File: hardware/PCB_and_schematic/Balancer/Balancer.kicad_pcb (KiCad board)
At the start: 2 copper layers, 99.5 x 99.5 mm, 164 parts, among them J1 BATT_OUT, J10 RS485, J11 HEATSING_TEMP1, J12 External Current Shunt, J13 BATT_IN, J2 Conn_01x04, J3 Conn_01x03, J4 HEATSING_TEMP1, J5 FAN1, J6 FAN2, J7 BATT_12V, J8 ICP, Q1 BC817, Q10 NPN, Q11 NPN, Q12 BC817, Q13 BD238, Q14 NPN, Q15 NPN, Q16 BD238, Q17 BC817, Q18 BC817, Q19 BC817, Q2 BC337, Q20 BC817, Q3 BC327, Q4 PMOS, Q5 PMOS, Q6 BC337, Q7 BC327, Q8 BC817, Q9 BC817, U1 LM324, U2 LM324, U3 LM358, U4 PIC16F886-IP, U5 TL431LP, U6 ST485, U7 INA226

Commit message: PCB UPDATE
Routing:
- net Net-(Q14-E): track 52.1 -> 52.9 mm
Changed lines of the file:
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@@
 			(xy 223.9518 54.9656) (xy 226.1616 54.9656) (xy 228.5238 57.3278) (xy 228.5238 66.1416) (xy 233.6292 71.247)
 			(xy 235.6866 71.247) (xy 235.7374 71.1962) (xy 235.7374 67.691) (xy 235.1278 67.691) (xy 232.1052 64.6684)
-			(xy 232.1052 59.8678) (xy 232.1306 59.8424) (xy 235.839 59.8424) (xy 235.839 57.3024) (xy 235.7882 57.2516)
+			(xy 232.1052 59.8678) (xy 232.1306 59.8424) (xy 232.119 59.8424) (xy 232.119 57.33) (xy 232.06 57.2516)
 			(xy 232.156 57.2516) (xy 232.1306 57.277) (xy 232.1052 57.2516) (xy 232.1052 55.8546) (xy 227.6348 51.3842)
 			(xy 224.0026 51.3842) (xy 223.901 51.4858) (xy 223.901 54.9148)
@@
 	)
 	(via
-		(at 209 54)
+		(at 209 55)
 		(size 6)
 		(drill 3.2)
@@
 	)
 	(segment
-		(start 176.8 138.7)
-		(end 176.8 136.05)
-		(width 1.5)
-		(layer "B.Cu")
-		(net 55)
-	)
-	(segment
 		(start 176.8 141.3)
 		(end 177.5 142)
@@
 	)
 	(segment
+		(start 176.8 135.25)
+		(end 176.85 135.2)
+		(width 1.5)
+		(layer "B.Cu")
+		(net 55)
+	)
+	(segment
 		(start 201.175 135.575)
 		(end 206.125 135.575)
@@
 	)
 	(segment
+		(start 176.8 138.7)
+		(end 176.8 135.25)
+		(width 1.5)
+		(layer "B.Cu")
+		(net 55)
+	)
+	(segment
 		(start 209.35 87.05)
 		(end 210.8 85.6)
@@
 	)
 	(segment
-		(start 181.85 131.5)
-		(end 169.4 131.5)
-		(width 3)
-		(layer "F.Cu")
-		(net 71)
-	)
-	(segment
 		(start 195.2 139.2)
 		(end 187.5 131.5)
@@
 	)
 	(segment
+		(start 181.85 131.5)
+		(end 169.4 131.5)
+		(width 3)
+		(layer "F.Cu")
+		(net 71)
+	)
+	(segment
 		(start 198.0184 144.9832)
 		(end 198 145.0016)
@@
 	)
 	(segment
-		(start 165.3 127.4)
-		(end 165.3 126.44)
-		(width 3)
+		(start 201.5528 144.7)
+		(end 204.0028 142.25)
+		(width 1.8)
 		(layer "F.Cu")
 		(net 71)
 	)
 	(segment
-		(start 201.5528 144.7)
-		(end 204.0028 142.25)
-		(width 1.8)
+		(start 165.3 127.4)
+		(end 165.3 126.44)
+		(width 3)
 		(layer "F.Cu")
 		(net 71)

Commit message: pcb update
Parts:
- added D23: LED, LED_SMD:LED_0805_2012Metric, F.Cu at (250.3, 90.0)
- added D5: LED, LED_SMD:LED_0805_2012Metric, F.Cu at (246.0, 90.1)
- added Q21: BC817, Package_TO_SOT_SMD:SOT-23, B.Cu at (246.8, 83.9)
- added Q22: BC817, Package_TO_SOT_SMD:SOT-23, B.Cu at (254.0, 90.0)
- added R77: 10K, Resistor_SMD:R_0805_2012Metric_Pad1.20x1.40mm_HandSolder, B.Cu at (246.8, 86.9)
- added R78: 220R, Resistor_SMD:R_0805_2012Metric_Pad1.20x1.40mm_HandSolder, B.Cu at (245.6, 89.0)
- added R79: 10K, Resistor_SMD:R_0805_2012Metric_Pad1.20x1.40mm_HandSolder, B.Cu at (249.6, 91.2)
- added R80: 220R, Resistor_SMD:R_0805_2012Metric_Pad1.20x1.40mm_HandSolder, B.Cu at (249.6, 89.0)
- MOD1: footprint My-Footprints-converters-modules:MP1584_Mini_3A_Step_Down_Conv -> My-Footprints-converters-modules:LM2596-Step-Down-Conv
- moved F4 44.7 mm to (223.1, 112.9), turned to 0 degrees
- moved MOD1 11.9 mm to (179.6, 136.3)
- moved R44 2.33 mm to (245.6, 91.2), turned to 0 degrees
- moved J10 1.70 mm to (193.9, 100.0)
- moved Q9 0.79 mm to (219.1, 121.8)
- moved R43 0.37 mm to (248.8, 93.4)
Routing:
- net +5V: track 216.8 -> 270.5 mm
- net RC0: track 16.8 -> 56.3 mm, vias 0 -> 2
- net RA6: track 14.8 -> 51.5 mm, vias 0 -> 2
- net Net-(Q21-C): track 0.00 -> 7.68 mm
- net Net-(Q22-C): track 0.00 -> 4.66 mm
- net Net-(Q22-B): track 0.00 -> 2.53 mm
- net Net-(Q21-B): track 0.00 -> 2.12 mm
- net +BATT_24V: track 222.9 -> 221.0 mm
- net Net-(D23-A): track 0.00 -> 1.81 mm, vias 0 -> 1
- net /BMS_microcontroller/RS485_A: track 19.2 -> 17.5 mm
- net Net-(MOD1-OUT+): track 6.83 -> 5.19 mm
- net Net-(Q14-B): track 46.6 -> 48.1 mm
- net /BMS_microcontroller/RS485_B: track 19.2 -> 18.0 mm
- net Net-(J5-Pin_1): track 31.2 -> 30.1 mm
- net Net-(Q9-B): track 2.18 -> 2.97 mm
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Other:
- board text added: "LM2596 Step Down Converter Module"

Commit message: PCB footprint changes
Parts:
- C1, C2: value 22u -> 100u/35V; footprint Capacitor_SMD:CP_Elec_6.3x4.9 -> Capacitor_THT:CP_Radial_D8.0mm_P3.50mm
- C14: value 47u/16V -> 470u/16V
- C15: value 47u -> 470u/16V
- C18: value 10u -> 100u/6,3V; footprint Capacitor_Tantalum_SMD:CP_EIA-7343-31_Kemet-D -> Capacitor_Tantalum_SMD:CP_EIA-3528-21_Kemet-B
- D23, D5: footprint LED_SMD:LED_0805_2012Metric -> LED_SMD:LED_PLCC-2_3.4x3.0mm_KA
- R74: value R -> 20A/75mV
- moved C18 4.19 mm to (204.9, 104.2)
- moved C2 2.20 mm to (228.6, 57.0)
- moved C1 2.02 mm to (175.4, 60.8)
- moved R74 0.67 mm to (198.6, 80.6)
- moved D23 0.18 mm to (250.5, 90.1)
- moved D5 0.14 mm to (246.1, 90.0)
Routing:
- net GNDA: track 321.5 -> 290.8 mm, vias 11 -> 9
- net DC_LINE_24V: track 40.4 -> 24.5 mm
- net PWM_OUT_DISCH: track 71.5 -> 65.1 mm
- net +5V: track 270.5 -> 268.7 mm
- net RA6: track 51.5 -> 52.8 mm
- net Net-(D5-A): track 0.62 -> 0.00 mm
- net GND: vias 47 -> 53
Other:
- board text added: "100u 35V"
- board text added: "470u/16V"

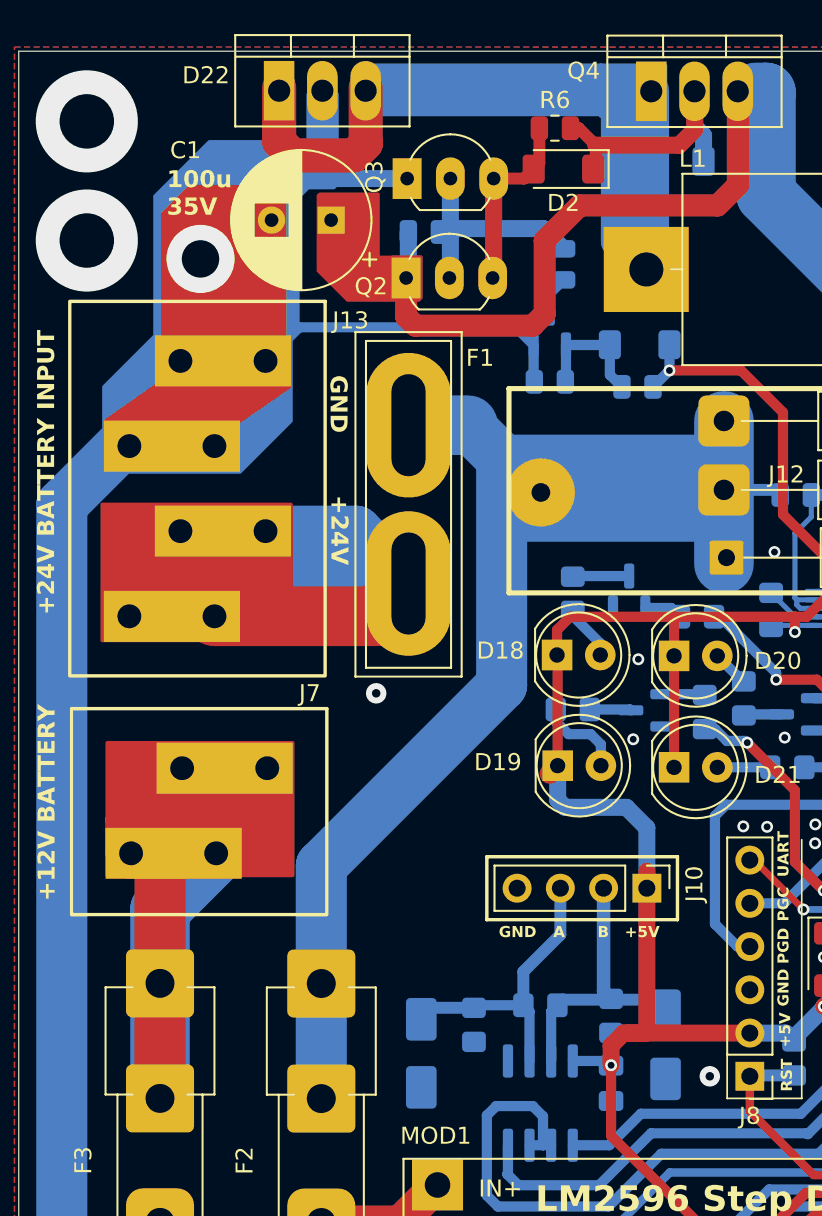
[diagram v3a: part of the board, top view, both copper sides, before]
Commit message: Update of ESP32 PCB - parts positioning
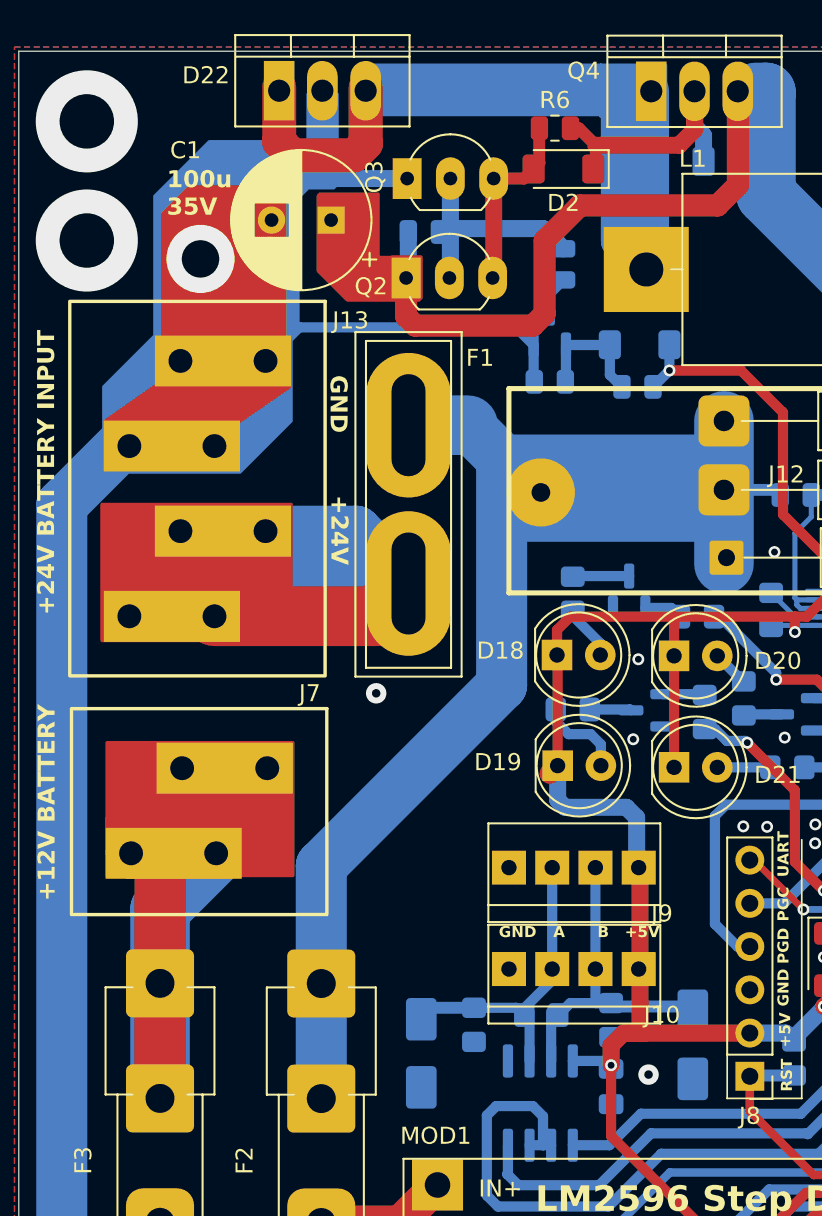
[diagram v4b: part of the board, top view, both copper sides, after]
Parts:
- added J9: RS485, My-Footprints-connectors:Conn-01x04-N25-W4P, F.Cu at (194.8, 102.0)
- J10: footprint Connector_PinHeader_2.54mm:PinHeader_1x04_P2.54mm_Vertical -> My-Footprints-connectors:Conn-01x04-N25-W4P
- moved J10 8.00 mm to (194.8, 108.0), turned to 180 degrees
- moved D17 1.60 mm to (196.6, 109.2)
- moved R52 0.58 mm to (187.7, 107.5)
- moved R51 0.25 mm to (191.8, 107.8)
- moved C20 0.19 mm to (191.8, 111.7)
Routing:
- net /BMS_microcontroller/RS485_B: track 18.0 -> 20.4 mm
- net /BMS_microcontroller/RS485_A: track 17.5 -> 19.0 mm
- net +5V: track 268.7 -> 267.5 mm

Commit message: Add SD card switcher circuit, some changes in pcb and schematic
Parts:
- moved D3 0.78 mm to (198.2, 57.3)
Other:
- board text added: "PIC16F886"
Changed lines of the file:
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@@
 		(tags "capacitor handsolder")
 		(property "Reference" "C8"
-			(at 2.8896 0.0484 -90)
+			(at 2.88 -0.18 -90)
 			(layer "B.SilkS")
 			(effects
@@
 		(tags "SO SO")
 		(property "Reference" "U3"
-			(at -4.4538 -1.7714 -90)
+			(at -3.455 -3.625 90)
 			(layer "B.SilkS")
 			(effects
@@
 		(tags "resistor handsolder")
 		(property "Reference" "R32"
-			(at 0.0476 -1.66 -90)
+			(at -6.14 2.43 -90)
 			(layer "B.SilkS")
 			(effects
@@
 		(tags "SOT TO_SOT_SMD")
 		(property "Reference" "Q22"
-			(at -0.0875 2.425 0)
+			(at 1.1875 2.375 0)
 			(layer "B.SilkS")
 			(effects
 				(font
-					(size 1 1)
+					(size 0.8 0.8)
 					(thickness 0.15)
 				)
@@
 		(tags "SOT TO_SOT_SMD")
 		(property "Reference" "Q21"
-			(at 0 2.4 -90)
+			(at 2.8 0.125 0)
 			(layer "B.SilkS")
 			(effects
@@
 	(footprint "Diode_SMD:D_MiniMELF"
 		(layer "B.Cu")
-		(at 198.98125 57.35 180)
+		(at 198.2 57.3 180)
 		(descr "Diode Mini-MELF (SOD-80)")
 		(tags "Diode Mini-MELF (SOD-80)")
@@
 		(tags "capacitor handsolder")
 		(property "Reference" "C12"
-			(at -3.3106 -0.0386 90)
+			(at 3.12 0.85 90)
 			(layer "B.SilkS")
 			(effects
 				(font
-					(size 1 1)
+					(size 0.8 0.8)
 					(thickness 0.15)
 				)
@@
 		(tags "resistor handsolder")
 		(property "Reference" "R44"
-			(at -2.5208 -0.0246 90)
+			(at -0.725 1.5 180)
 			(layer "B.SilkS")
 			(effects
 				(font
-					(size 1 1)
+					(size 0.8 0.8)
 					(thickness 0.15)
 				)
@@
 		(tags "resistor handsolder")
 		(property "Reference" "R39"
-			(at 2.5698 0.3206 -90)
+			(at 2.64 0.53 -90)
 			(layer "B.SilkS")
 			(effects
@@
 		(tags "resistor handsolder")
 		(property "Reference" "R77"
-			(at 0 1.65 180)
+			(at -2.6 6.125 -90)
 			(layer "B.SilkS")
 			(effects
@@
 		(tags "resistor handsolder")
 		(property "Reference" "R78"
-			(at 0 1.65 0)
+			(at -1.475 -2.5 90)
 			(layer "B.SilkS")
 			(effects
@@
 		(tags "Diode Mini-MELF (SOD-80)")
 		(property "Reference" "D6"
-			(at -3.741 -0.054 180)
+			(at -0.4 -1.9 180)
 			(layer "B.SilkS")
 			(effects
@@
 		(tags "resistor handsolder")
 		(property "Reference" "R43"
-			(at 2.5906 0.1034 90)
+			(at 2.475 0.075 -90)
 			(layer "B.SilkS")
 			(effects
 				(font
-					(size 1 1)
+					(size 0.8 0.8)
 					(thickness 0.15)
 				)
@@
 		(tags "SOIC SO")
 		(property "Reference" "U4"
-			(at 4.5 18.4 180)
+			(at -4.8 10.15 180)
 			(layer "B.SilkS")
 			(effects
@@
 		(tags "resistor handsolder")
 		(property "Reference" "R79"
-			(at 0 1.65 180)
+			(at -3.275 -1.15 180)
 			(layer "B.SilkS")
 			(effects
 				(font
-					(size 1 1)
+					(size 0.8 0.8)
 					(thickness 0.15)
 				)
@@
 		(net 72)
 	)
+	(gr_line
+		(start 249.375 85.65)
+		(end 248.7 86.325)
+		(stroke
+			(width 0.1)
+			(type default)
+		)
+		(layer "B.SilkS")
+	)
+	(gr_rect
+		(start 238.85 83.6)
+		(end 240.6 86.6)
+		(stroke
+			(width 0.1)
+			(type default)
+		)
+		(fill none)
+		(layer "B.SilkS")
+	)
 	(gr_rect
 		(start 169 128.9)
@@
 	)
 	(gr_line
+		(start 240.6 86.6)
+		(end 240.6 88.35)
+		(stroke
+			(width 0.1)
+			(type default)
+		)
+		(layer "B.SilkS")
+	)
+	(gr_line
+		(start 240.6 88.35)
+		(end 241.6 89.35)
+		(stroke
+			(width 0.1)
+			(type default)
+		)
+		(layer "B.SilkS")
+	)
+	(gr_line
+		(start 249.375 82.35)
+		(end 249.375 85.65)
+		(stroke
+			(width 0.1)
+			(type default)
+		)
+		(layer "B.SilkS")
+	)
+	(gr_rect
+		(start 248.65 79.25)
+		(end 250.1 82.35)
+		(stroke
+			(width 0.1)
+			(type default)
+		)
+		(fill none)
+		(layer "B.SilkS")
+	)
+	(gr_line
 		(start 198.62 109.83)
 		(end 198.62 112.4)
@@
 		(layer "Edge.Cuts")
 	)
+	(gr_text "PIC16F886"
+		(at 216.5 100.5 90)
+		(layer "B.SilkS")
+		(effects
+			(font
+				(size 1 1)
+				(thickness 0.2)
+				(bold yes)
+			)
+			(justify left bottom mirror)
+		)
+	)
 	(gr_text "GROUNDS\nCONNECTION\nPOINT"
 		(at 174.4 132 0)
@@
 	)
 	(via
-		(at 255.4 92)
+		(at 255.7 93.65)
 		(size 0.7)
 		(drill 0.4)
@@
 	)
 	(via
-		(at 249.1 83.1)
+		(at 250.85 80.8)
 		(size 0.7)
 		(drill 0.4)
@@
 	)
 	(segment
-		(start 197.23125 56.9125)
-		(end 197.23125 55.83125)
+		(start 196.71 55.31)
+		(end 196.71 53)
 		(width 1)
 		(layer "B.Cu")
@@
 	)
 	(segment
-		(start 196.71 55.31)
-		(end 196.71 53)
+		(start 196.45 57.3)
+		(end 196.45 55.57)
 		(width 1)
 		(layer "B.Cu")
@@
 	)
 	(segment
-		(start 197.23125 55.83125)
+		(start 196.45 55.57)
 		(end 196.71 55.31)
 		(width 1)

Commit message: progress with esp power pcb
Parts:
- added G***: LOGO, graphic:honeybadger2, F.Cu at (241.2, 119.2)

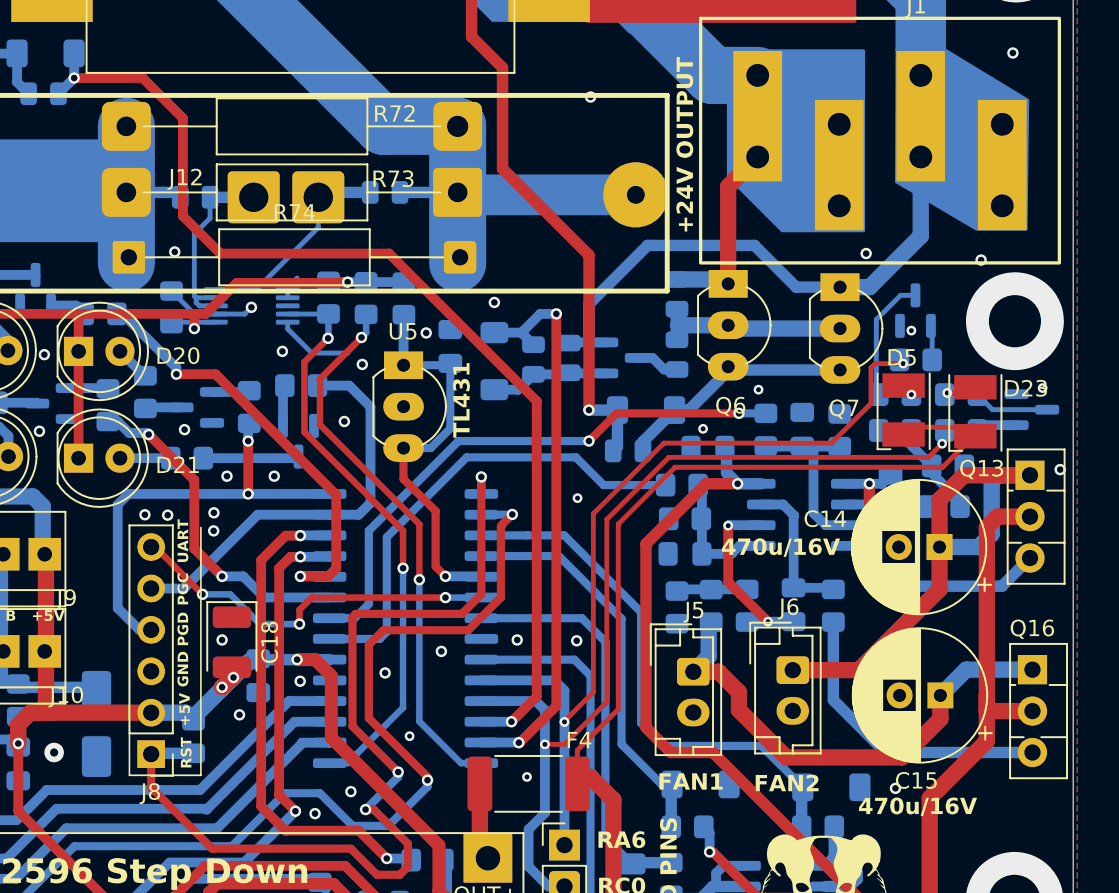
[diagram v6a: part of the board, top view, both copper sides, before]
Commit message: Parts chage for bms
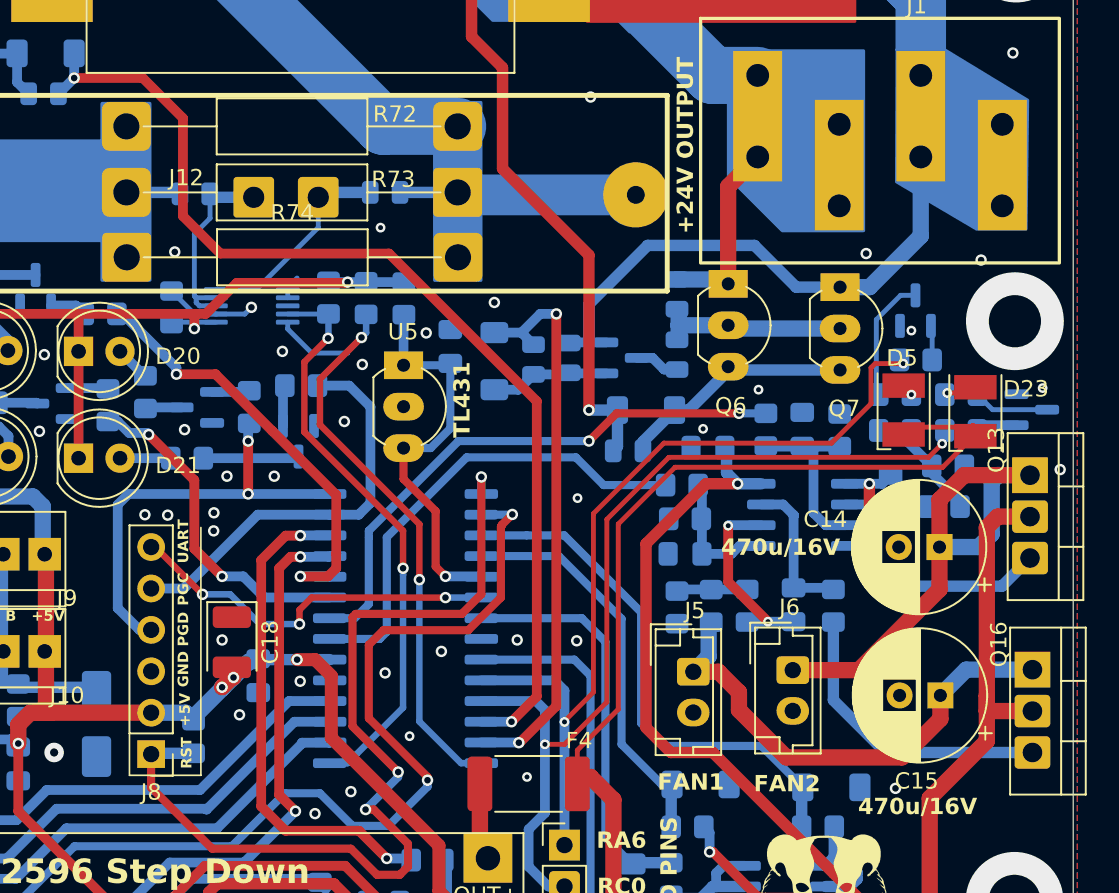
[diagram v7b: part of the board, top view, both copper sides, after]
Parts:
- C18: value 100u/6,3V -> 100u/6,3V (JA8)
- Q13, Q16: footprint Package_TO_SOT_THT:TO-126-3_Vertical -> My-Footprints:TO-220-3_Vertical-little-bigger pads
- moved R75 0.21 mm to (202.6, 76.7)
- moved R74 0.13 mm to (198.4, 80.6)
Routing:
- net Net-(F1-Pad2): track 71.4 -> 63.0 mm
- net Net-(D3-K): track 95.3 -> 86.9 mm
- net GND: vias 53 -> 54
